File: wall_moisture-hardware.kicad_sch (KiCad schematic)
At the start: 0 parts

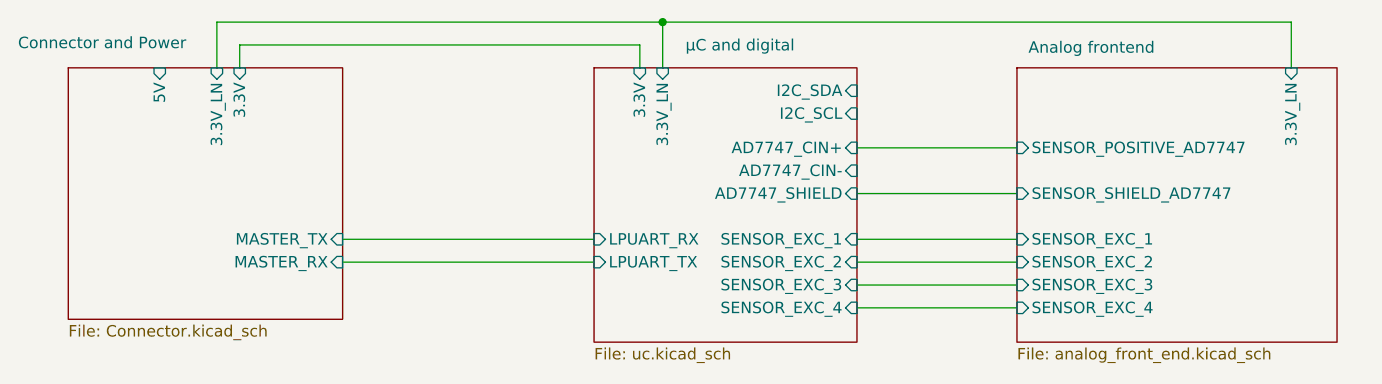
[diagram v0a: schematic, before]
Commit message: rule-check: Fix the ERC errors and warnings
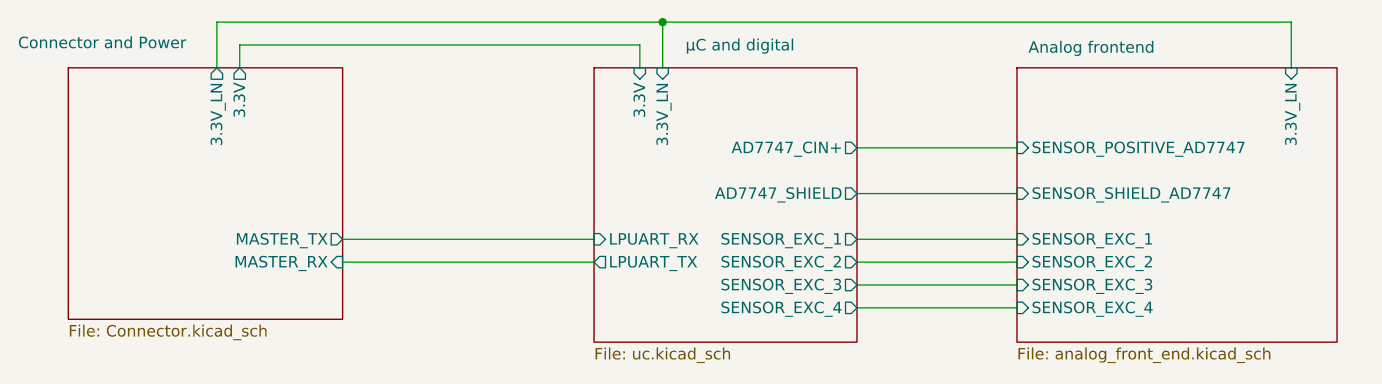
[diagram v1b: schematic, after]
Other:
- sheet Connector and Power ports: added none; removed 5V
- sheet µC and digital ports: added none; removed AD7747_CIN-, I2C_SCL, I2C_SDA
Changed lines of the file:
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@@
-			)
-		)
-		(pin "I2C_SDA" input
-			(at 125.73 106.68 0)
-			(effects
-				(font
-					(size 1.27 1.27)
-				)
-				(justify right)
-			)
-		)
-		(pin "I2C_SCL" input
-			(at 125.73 109.22 0)
-			(effects
-				(font
-					(size 1.27 1.27)
-				)
-				(justify right)
 			)
 		)
@@
 			)
 		)
-		(pin "LPUART_TX" input
+		(pin "LPUART_TX" output
 			(at 96.52 125.73 180)
 			(effects
@@
 			)
 		)
-		(pin "AD7747_SHIELD" input
+		(pin "AD7747_SHIELD" output
 			(at 125.73 118.11 0)
 			(effects
@@
 			)
 		)
-		(pin "AD7747_CIN+" input
+		(pin "AD7747_CIN+" output
 			(at 125.73 113.03 0)
 			(effects
@@
 			)
 		)
-		(pin "AD7747_CIN-" input
-			(at 125.73 115.57 0)
-			(effects
-				(font
-					(size 1.27 1.27)
-				)
-				(justify right)
-			)
-		)
-		(pin "SENSOR_EXC_1" input
+		(pin "SENSOR_EXC_1" output
 			(at 125.73 123.19 0)
 			(effects
@@
 			)
 		)
-		(pin "SENSOR_EXC_2" input
+		(pin "SENSOR_EXC_2" output
 			(at 125.73 125.73 0)
 			(effects
@@
 			)
 		)
-		(pin "SENSOR_EXC_3" input
+		(pin "SENSOR_EXC_3" output
 			(at 125.73 128.27 0)
 			(effects
@@
 			)
 		)
-		(pin "SENSOR_EXC_4" input
+		(pin "SENSOR_EXC_4" output
 			(at 125.73 130.81 0)
 			(effects
@@
 			)
 		)
-		(pin "5V" input
-			(at 48.26 104.14 90)
-			(effects
-				(font
-					(size 1.27 1.27)
-				)
-				(justify right)
-			)
-		)
 		(pin "MASTER_RX" input
 			(at 68.58 125.73 0)
@@
 			)
 		)
-		(pin "MASTER_TX" input
+		(pin "MASTER_TX" output
 			(at 68.58 123.19 0)
 			(effects
@@
 			)
 		)
-		(pin "3.3V" input
+		(pin "3.3V" output
 			(at 57.15 104.14 90)
 			(effects
@@
 			)
 		)
-		(pin "3.3V_LN" input
+		(pin "3.3V_LN" output
 			(at 54.61 104.14 90)
 			(effects

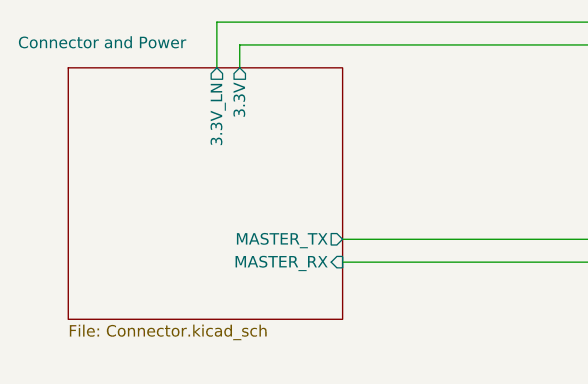
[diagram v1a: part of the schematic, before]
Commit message: chore: fix the naming of connectors sheet file name and the change the path of footprints
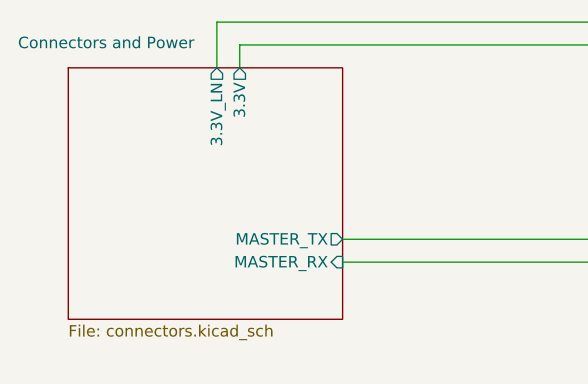
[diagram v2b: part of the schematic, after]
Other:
- sheet Connector and Power renamed Connectors and Power
- sheet Connectors and Power: file Connector.kicad_sch -> connectors.kicad_sch
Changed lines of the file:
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@@
 			(color 0 0 0 0.0000)
 		)
-		(property "Sheetname" "Connector and Power"
+		(property "Sheetname" "Connectors and Power"
 			(at 32.512 102.108 0)
 			(effects
@@
 			)
 		)
-		(property "Sheetfile" "Connector.kicad_sch"
+		(property "Sheetfile" "connectors.kicad_sch"
 			(at 38.1 132.6646 0)
 			(effects

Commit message: design: Assign the project version and project company from project variable, which are then substituted during the ci
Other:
- company: Micka Inc -> ${COMPANY}
- title: Wall Moisture Sensor (WMS1) -> Wall Moisture Sensor - WMS1
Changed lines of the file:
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@@
 	(paper "A4")
 	(title_block
-		(title "Wall Moisture Sensor (WMS1)")
-		(rev "r1")
-		(company "Micka Inc")
+		(title "Wall Moisture Sensor - WMS1")
+		(rev "${VERSION}")
+		(company "${COMPANY}")
 	)
 	(junction
